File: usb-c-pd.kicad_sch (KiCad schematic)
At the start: 36 parts, among them J1 USB_C_Receptacle_PowerOnly_6P, J2 Barrel_Jack_Switch, Q1 T2N7002AK, U1 CYPD3177-24LQ, U2 STM32G030K8Tx, U3 INA180A3

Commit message: feat: stm mcu
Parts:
- removed U2: STM32G030K8Tx, Package_QFP:LQFP-32_7x7mm_P0.8mm, symbol MCU_ST_STM32G0:STM32G030K8Tx
- removed U3: INA180A3, Package_TO_SOT_SMD:SOT-23-5, symbol Amplifier_Current:INA180A3
- added C10: 100nF, symbol Device:C_Small
- added C11: 0.1uF, symbol Device:C_Small
- added C12: 4.7uF, symbol Device:C_Small
- added C13: 470uF, symbol Device:C_Small
- added C14: 1uF, symbol Device:C_Small
- added C15: 180uF, symbol Device:C_Small
- added D2: LED, symbol Device:LED
- added D3: 1N5820, Diode_THT:D_DO-201AD_P15.24mm_Horizontal, symbol Diode:1N5820
- added J3: TC2030, Connector:Tag-Connect_TC2030-IDC-NL_2x03_P1.27mm_Vertical, symbol Connector:TC2030
- added L1: 68uH, symbol Device:L
- added R20, R21: 20k, symbol Device:R_Small
- added R22: 2.2k, symbol Device:R_Small
- added R23: TODO, symbol Device:R_Small
- added U2: STM32C071F8Px, Package_SO:TSSOP-20_4.4x6.5mm_P0.65mm, symbol MCU_ST_STM32C0:STM32C071F8Px
- added U3: INA180A2, Package_TO_SOT_SMD:SOT-23-5, symbol Amplifier_Current:INA180A2
- added U4: XL1509-3.3, Package_SO:SOIC-8_3.9x4.9mm_P1.27mm, symbol Regulator_Switching:XL1509-3.3
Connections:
- net +3V3 MCU: now also C11.1, C12.1, C15.1, L1.2, U2.4 (VDD), U3.5 (V+), U4.3 (FB)
- net +VBUS_PD: now also U3.3 (+)
- net AMP_OUT: now also U2.8 (PA1)
- net GND: now also C10.2, C11.2, C12.2, C13.2, C14.2, C15.2, D3.2 (A), R22.2, R23.1, U2.5 (VSS), U3.2 (GND), U4.5 (GND), U4.6 (GND), U4.7 (GND), U4.8 (GND)
- net PD_SAFE: now also U2.6 (PF2)
- net VBUS: now also C13.1, C14.1, U4.1 (VIN)
- net VCONN: now also R20.1, R21.1, U3.4 (-)
- net I2C2_SDA: now reaches R4.2, U1.12 (HPI_SDA)
- net I2C2_SDA: now also U2.13 (PA6)
- net at R19.1: now also U3.1
- net I2C2_SCL: now reaches R3.2, U1.13 (HPI_SCL)
- net I2C2_SCL: now also U2.14 (PA7)
- net HPI_INT: now reaches U1.7 (~{HPI_INT})
- net HPI_INT: now also U2.3 (PC15)
- net PD_GPIO: now reaches U1.8 (GPIO_1)
- net PD_GPIO: now also U2.2 (PC14)
- new net: C10.1, R20.2, R21.2, R22.1, U2.7 (PA0)
- new net: D2.1 (K), R23.2
- new net: D2.2 (A), U2.1 (PB7/PB8)
- new net: D3.1 (K), L1.1, U4.2 (OUT)
- new net SWCLK: U2.19 (PA14/PA15)
- new net SWDIO: U2.18 (PA13)
- new net USB_DM: U2.16 (PA11)
- new net USB_DP: U2.17 (PA12)
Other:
- note added: "STATUS"
- note removed: "Verify that this transistor is in stock"
- moved on the sheet: D1

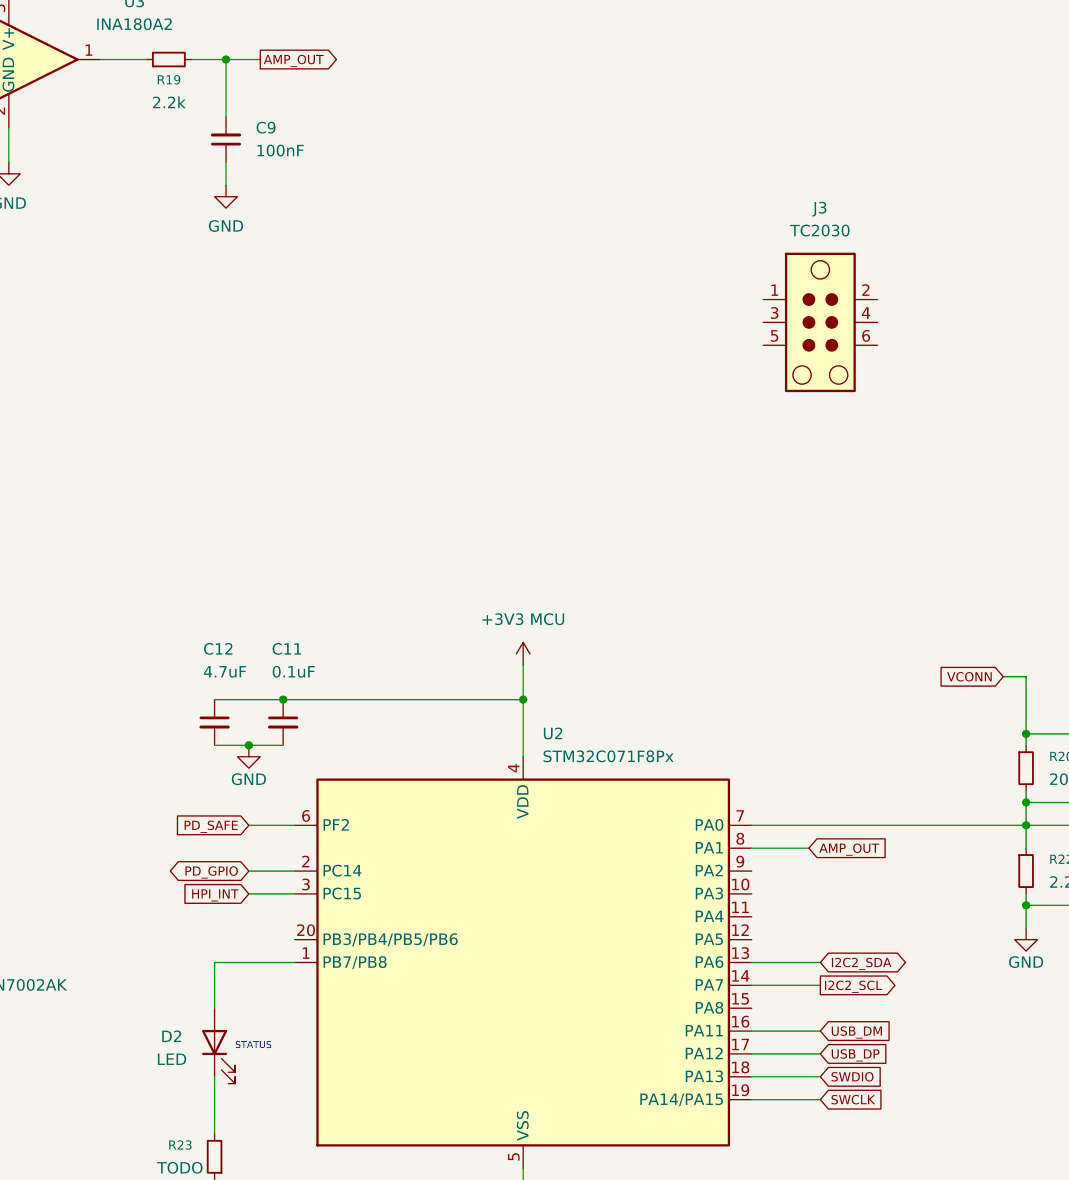
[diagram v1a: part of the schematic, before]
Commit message: feat: SWO programming
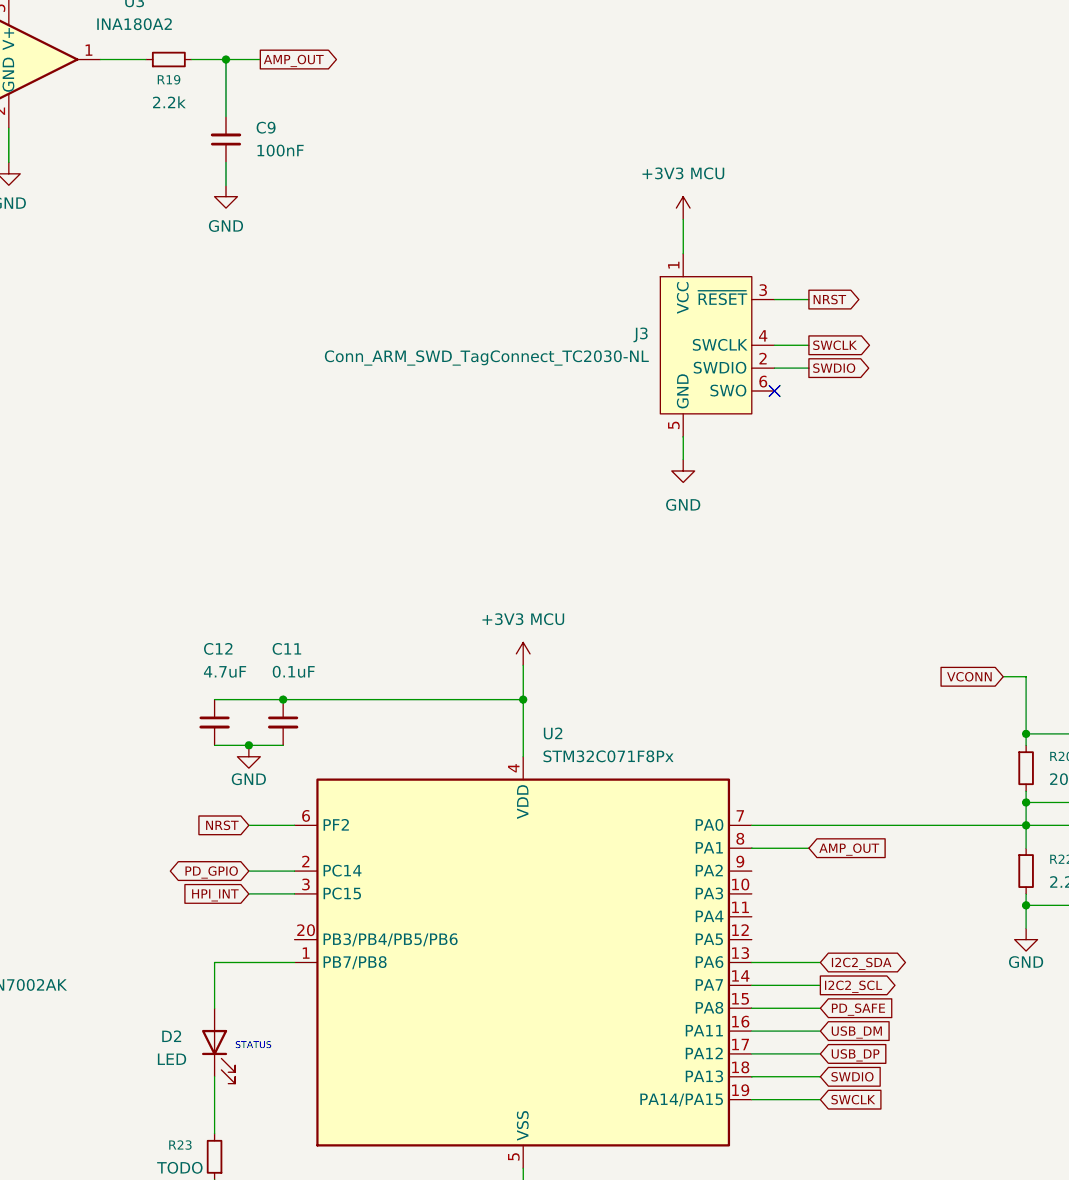
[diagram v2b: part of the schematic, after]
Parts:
- removed J3: TC2030, Connector:Tag-Connect_TC2030-IDC-NL_2x03_P1.27mm_Vertical, symbol Connector:TC2030
- added J3: Conn_ARM_SWD_TagConnect_TC2030-NL, Connector:Tag-Connect_TC2030-IDC-NL_2x03_P1.27mm_Vertical, symbol Connector:Conn_ARM_SWD_TagConnect_TC2030-NL
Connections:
- net +3V3 MCU: now also J3.1 (VCC)
- net GND: now also J3.5 (GND)
- net PD_SAFE: now also U2.15 (PA8); no longer U2.6 (PF2)
- net SWCLK: now also J3.4 (SWCLK)
- net SWDIO: now also J3.2 (SWDIO)
- new net NRST: J3.3 (~{RESET}), U2.6 (PF2)
- no-connect marks 0 -> 1

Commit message: verify ERC
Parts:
- removed J1: USB_C_Receptacle_PowerOnly_6P, symbol Connector:USB_C_Receptacle_PowerOnly_6P
- added J4: USB_C_Receptacle_USB2.0_14P, symbol Connector:USB_C_Receptacle_USB2.0_14P
- R1, R3, R4: value 4.7k -> 2.2k; footprint (none) -> Resistor_SMD:R_0603_1608Metric_Pad0.98x0.95mm_HandSolder
- R10, R11, R13, R14, R15, R16, R17, R19, R2, R20, R21, R22, R23, R5, R6, R7, R8, R9: footprint (none) -> Resistor_SMD:R_0603_1608Metric_Pad0.98x0.95mm_HandSolder
- R12: value DNP -> 2.2k; footprint (none) -> Resistor_SMD:R_0603_1608Metric_Pad0.98x0.95mm_HandSolder
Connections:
- net GND: now also U4.4 (~{EN}), J4.A1 (GND), J4.A12 (GND), J4.B1 (GND), J4.B12 (GND), J4.S1 (SHIELD)
- net USB_DM: now also J4.A7 (D-), J4.B7 (D-)
- net USB_DP: now also J4.A6 (D+), J4.B6 (D+)
- net VBUS: now also J4.A4 (VBUS), J4.A9 (VBUS), J4.B4 (VBUS), J4.B9 (VBUS)
- net +1V8: now reaches C1.1, U1.24 (VCCD)
- net PD_FLIP: now reaches R1.1, U1.10 (FLIP)
- net PD_FLIP: now also U2.12 (PA5)
- net at U1.14 (CC2): now also J4.B5 (CC2)
- net at U1.15 (CC1): now also J4.A5 (CC1)
- no-connect marks 1 -> 5
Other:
- note added: "verify this"
- moved on the sheet: C1

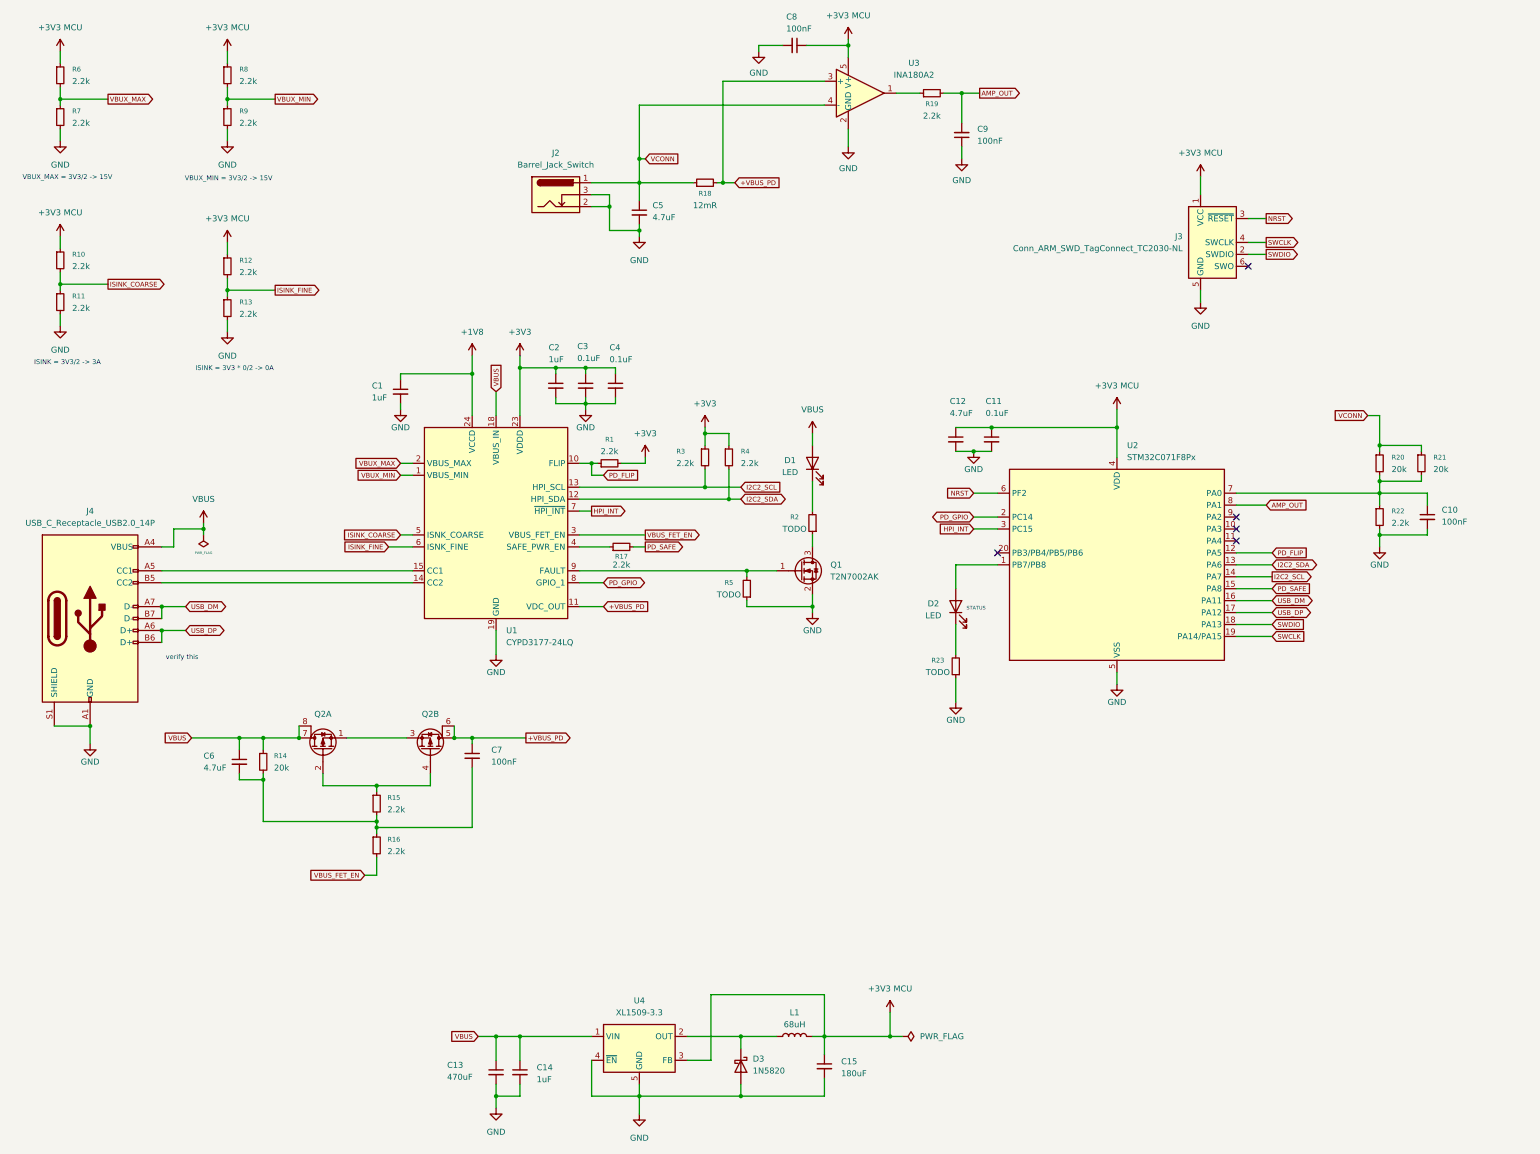
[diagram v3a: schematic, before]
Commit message: feat: configure footprints (#2)
* feat: stm mcu

* feat: SWO programming

* verify ERC

* feat: configure footprints
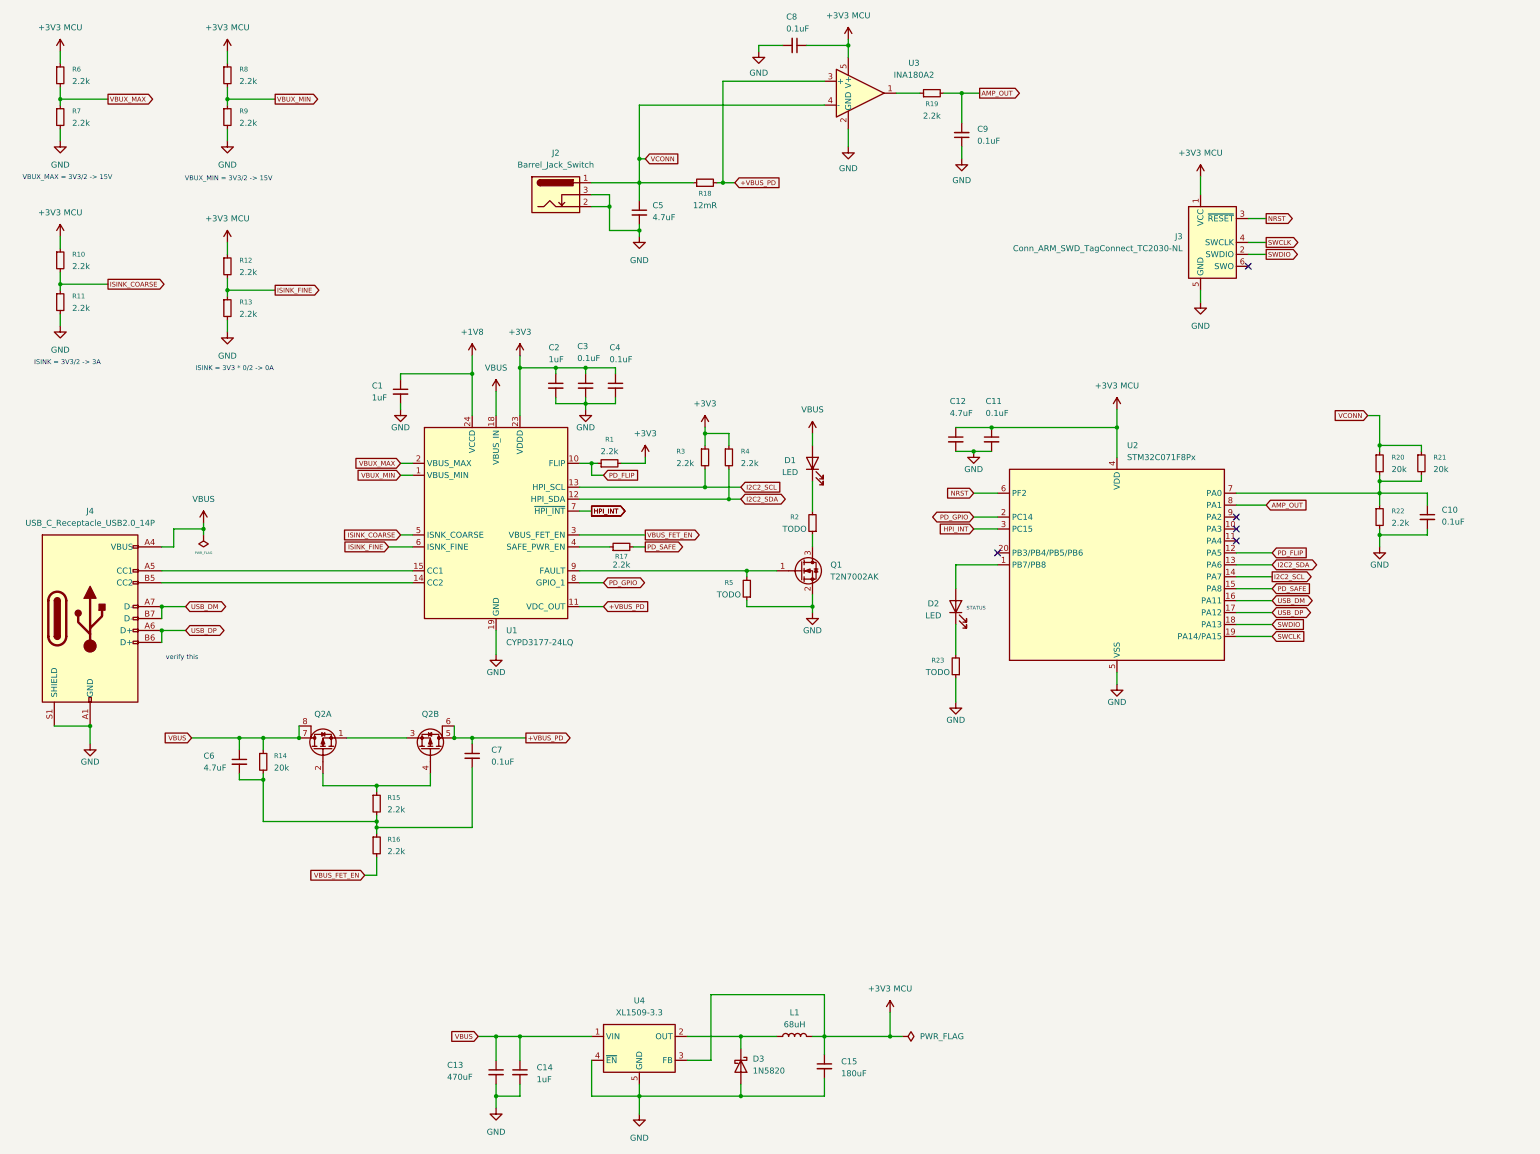
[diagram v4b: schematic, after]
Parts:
- C1, C11, C12, C13, C14, C15, C2, C3, C4, C5, C6: footprint (none) -> Capacitor_SMD:C_0603_1608Metric_Pad1.08x0.95mm_HandSolder
- C10, C7, C8, C9: value 100nF -> 0.1uF; footprint (none) -> Capacitor_SMD:C_0603_1608Metric_Pad1.08x0.95mm_HandSolder
- D1, D2: footprint (none) -> Diode_SMD:D_0603_1608Metric_Pad1.05x0.95mm_HandSolder
- J2: footprint (none) -> usb-c-pd-lib:PJ002AHSMTTR
- L1: footprint (none) -> Inductor_SMD:L_0603_1608Metric_Pad1.05x0.95mm_HandSolder
- R18: footprint (none) -> Resistor_SMD:R_0603_1608Metric_Pad0.98x0.95mm_HandSolder
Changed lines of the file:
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@@
 		)
 	)
-	(global_label "VBUS"
-		(shape input)
-		(at 119.38 97.79 90)
+	(global_label "HPI_INT"
+		(shape output)
+		(at 139.7 123.19 0)
 		(fields_autoplaced yes)
 		(effects
@@
 		)
 		(property "Intersheetrefs" "${INTERSHEET_REFS}"
-			(at 119.38 91.4832 90)
+			(at 147.7485 123.19 0)
 			(effects
 				(font
@@
 			)
 		)
-		(property "Footprint" ""
+		(property "Footprint" "Capacitor_SMD:C_0603_1608Metric_Pad1.08x0.95mm_HandSolder"
 			(at 138.43 96.52 0)
 			(effects
@@
 			)
 		)
-		(property "Footprint" ""
+		(property "Footprint" "Capacitor_SMD:C_0603_1608Metric_Pad1.08x0.95mm_HandSolder"
 			(at 99.06 97.79 0)
 			(effects
@@
 			)
 		)
-		(property "Footprint" ""
+		(property "Footprint" "Diode_SMD:D_0603_1608Metric_Pad1.05x0.95mm_HandSolder"
 			(at 217.17 143.51 0)
 			(effects
@@
 			)
 		)
-		(property "Value" "100nF"
+		(property "Value" "0.1uF"
 			(at 181.102 20.574 90)
 			(effects
@@
 			)
 		)
-		(property "Footprint" ""
+		(property "Footprint" "Capacitor_SMD:C_0603_1608Metric_Pad1.08x0.95mm_HandSolder"
 			(at 182.88 24.13 0)
 			(effects
@@
 			)
 		)
-		(property "Value" "100nF"
+		(property "Value" "0.1uF"
 			(at 320.548 125.476 0)
 			(effects
@@
 			)
 		)
-		(property "Footprint" ""
+		(property "Footprint" "Capacitor_SMD:C_0603_1608Metric_Pad1.08x0.95mm_HandSolder"
 			(at 317.5 124.46 0)
 			(effects
@@
 			)
 		)
-		(property "Footprint" ""
+		(property "Footprint" "Capacitor_SMD:C_0603_1608Metric_Pad1.08x0.95mm_HandSolder"
 			(at 217.17 107.95 0)
 			(effects
@@
 			)
 		)
-		(property "Footprint" ""
+		(property "Footprint" "Capacitor_SMD:C_0603_1608Metric_Pad1.08x0.95mm_HandSolder"
 			(at 132.08 96.52 0)
 			(effects
@@
 			)
 		)
-		(property "Footprint" ""
+		(property "Footprint" "Capacitor_SMD:C_0603_1608Metric_Pad1.08x0.95mm_HandSolder"
 			(at 189.23 241.3 0)
 			(effects
@@
 			)
 		)
-		(property "Footprint" ""
+		(property "Footprint" "Capacitor_SMD:C_0603_1608Metric_Pad1.08x0.95mm_HandSolder"
 			(at 119.38 242.57 0)
 			(effects
@@
 			)
 		)
-		(property "Footprint" ""
+		(property "Footprint" "Capacitor_SMD:C_0603_1608Metric_Pad1.08x0.95mm_HandSolder"
 			(at 144.78 96.52 0)
 			(effects
@@
 	)
 	(symbol
+		(lib_id "power:VBUS")
+		(at 119.38 97.79 0)
+		(unit 1)
+		(exclude_from_sim no)
+		(in_bom yes)
+		(on_board yes)
+		(dnp no)
+		(fields_autoplaced yes)
+		(property "Reference" "#PWR035"
+			(at 119.38 101.6 0)
+			(effects
+				(font
+					(size 1.27 1.27)
+				)
+				(hide yes)
+			)
+		)
+		(property "Value" "VBUS"
+			(at 119.38 92.71 0)
+			(effects
+				(font
+					(size 1.27 1.27)
+				)
+			)
+		)
+		(property "Footprint" ""
+			(at 119.38 97.79 0)
+			(effects
+				(font
+					(size 1.27 1.27)
+				)
+				(hide yes)
+			)
+		)
+		(property "Datasheet" ""
+			(at 119.38 97.79 0)
+			(effects
+				(font
+					(size 1.27 1.27)
+				)
+				(hide yes)
+			)
+		)
+		(property "Description" "Power symbol creates a global label with name \"VBUS\""
+			(at 119.38 97.79 0)
+			(effects
+				(font
+					(size 1.27 1.27)
+				)
+				(hide yes)
+			)
+		)
+		(pin "1"
+		)
+		(instances
+			(project "usb-c-pd"
+				(path "/8b91f438-df16-4abb-b457-7ba42e3c4b7f"
+					(reference "#PWR035")
+					(unit 1)
+				)
+			)
+		)
+	)
+	(symbol
 		(lib_id "Connector:USB_C_Receptacle_USB2.0_14P")
 		(at 33.02 146.05 0)
@@
 			)
 		)
-		(property "Value" "100nF"
+		(property "Value" "0.1uF"
 			(at 118.364 176.53 0)
 			(effects
@@
 			)
 		)
-		(property "Footprint" ""
+		(property "Footprint" "Capacitor_SMD:C_0603_1608Metric_Pad1.08x0.95mm_HandSolder"
 			(at 114.3 175.26 0)
 			(effects
@@
 			)
 		)
-		(property "Footprint" ""
+		(property "Footprint" "usb-c-pd-lib:PJ002AHSMTTR"
 			(at 133.35 56.896 0)
 			(effects
@@
 			)
 		)
-		(property "Footprint" ""
+		(property "Footprint" "Inductor_SMD:L_0603_1608Metric_Pad1.05x0.95mm_HandSolder"
 			(at 182.88 234.95 0)
 			(effects
@@
 			)
 		)
-		(property "Footprint" ""
+		(property "Footprint" "Capacitor_SMD:C_0603_1608Metric_Pad1.08x0.95mm_HandSolder"
 			(at 224.79 107.95 0)
 			(effects
@@
 			)
 		)
-		(property "Footprint" ""
+		(property "Footprint" "Capacitor_SMD:C_0603_1608Metric_Pad1.08x0.95mm_HandSolder"
 			(at 124.46 242.57 0)
 			(effects
@@
 			)
 		)
-		(property "Footprint" ""
+		(property "Footprint" "Diode_SMD:D_0603_1608Metric_Pad1.05x0.95mm_HandSolder"
 			(at 186.69 113.03 0)
 			(effects
@@
 			)
 		)
-		(property "Value" "100nF"
+		(property "Value" "0.1uF"
 			(at 221.742 44.45 0)
 			(effects
@@
 			)
 		)
-		(property "Footprint" ""
+		(property "Footprint" "Capacitor_SMD:C_0603_1608Metric_Pad1.08x0.95mm_HandSolder"
 			(at 218.44 43.18 0)
 			(effects
@@
 			)
 		)
-		(property "Footprint" ""
+		(property "Footprint" "Capacitor_SMD:C_0603_1608Metric_Pad1.08x0.95mm_HandSolder"
 			(at 64.77 176.53 0)
 			(effects
@@
 			)
 		)
-		(property "Footprint" ""
+		(property "Footprint" "Capacitor_SMD:C_0603_1608Metric_Pad1.08x0.95mm_HandSolder"
 			(at 149.86 59.69 0)
 			(effects
@@
 			)
 		)
-		(property "Footprint" ""
+		(property "Footprint" "Resistor_SMD:R_0603_1608Metric_Pad0.98x0.95mm_HandSolder"
 			(at 163.83 53.34 0)
 			(effects
